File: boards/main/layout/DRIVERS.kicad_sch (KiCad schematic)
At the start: 28 parts, among them IC5 L6205D013TR, IC6 STSPIN958TR, M1 B02B-PASK(LF)(SN), M2 B02B-PASK(LF)(SN), M3 B02B-PASK(LF)(SN)

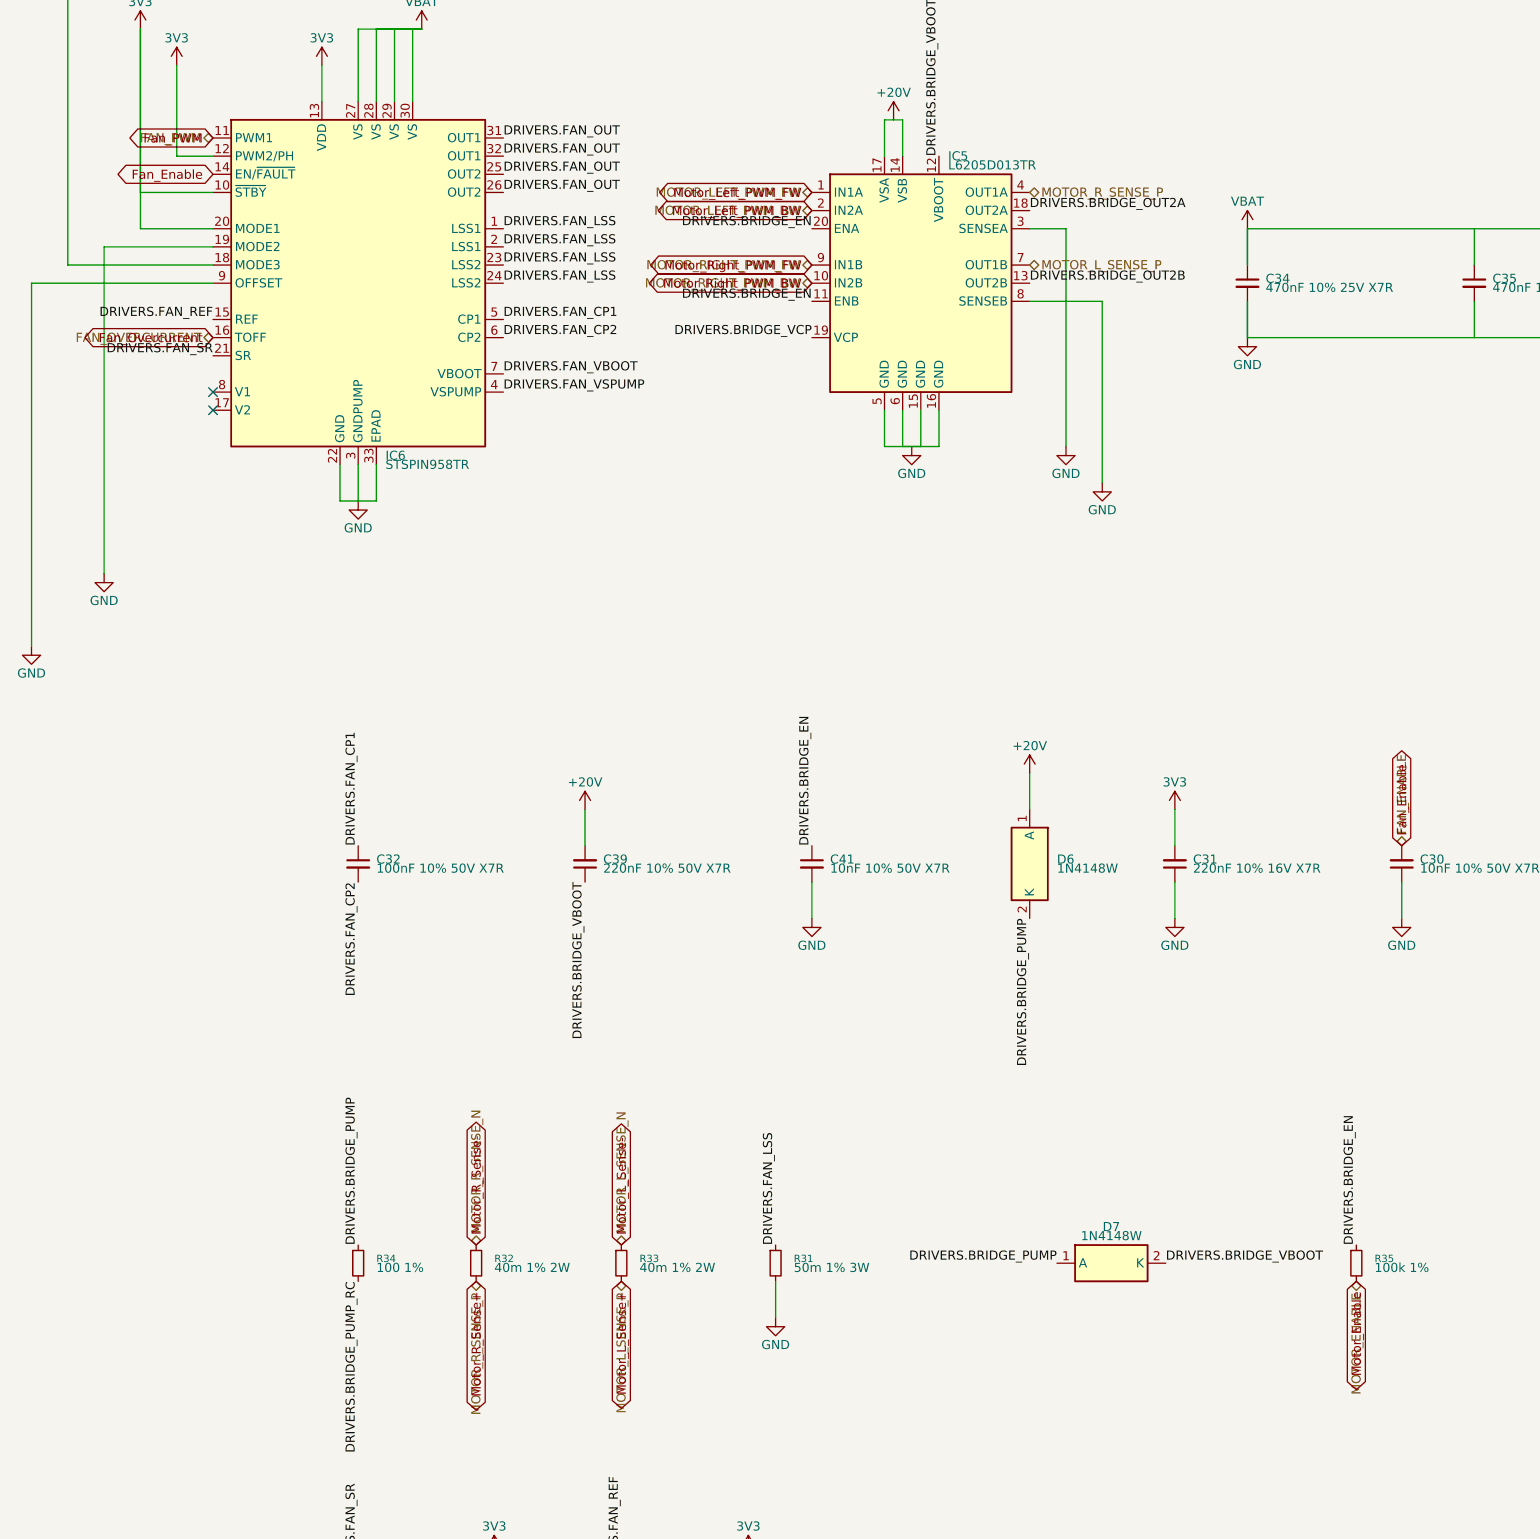
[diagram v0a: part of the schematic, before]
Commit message: 🏷️ Name the main board's module ports after their nets
A module's signal port now takes the name of the board net it carries (Fan_Enable, Wall_Sensor_0, Button), so its sheet pin and hierarchical label match the root's label: KiCad's ERC flagged each pair as similar_labels, names that differ only in case. The SPI buses and the Motor_*_Sense+/- nets, whose names are not identifiers, keep their port names. GND_BAT becomes a ground port of REGULATORS, so it reaches the root as a power symbol at the sheet pin instead of a dangling label. The netlist is unchanged: same nets, same names.
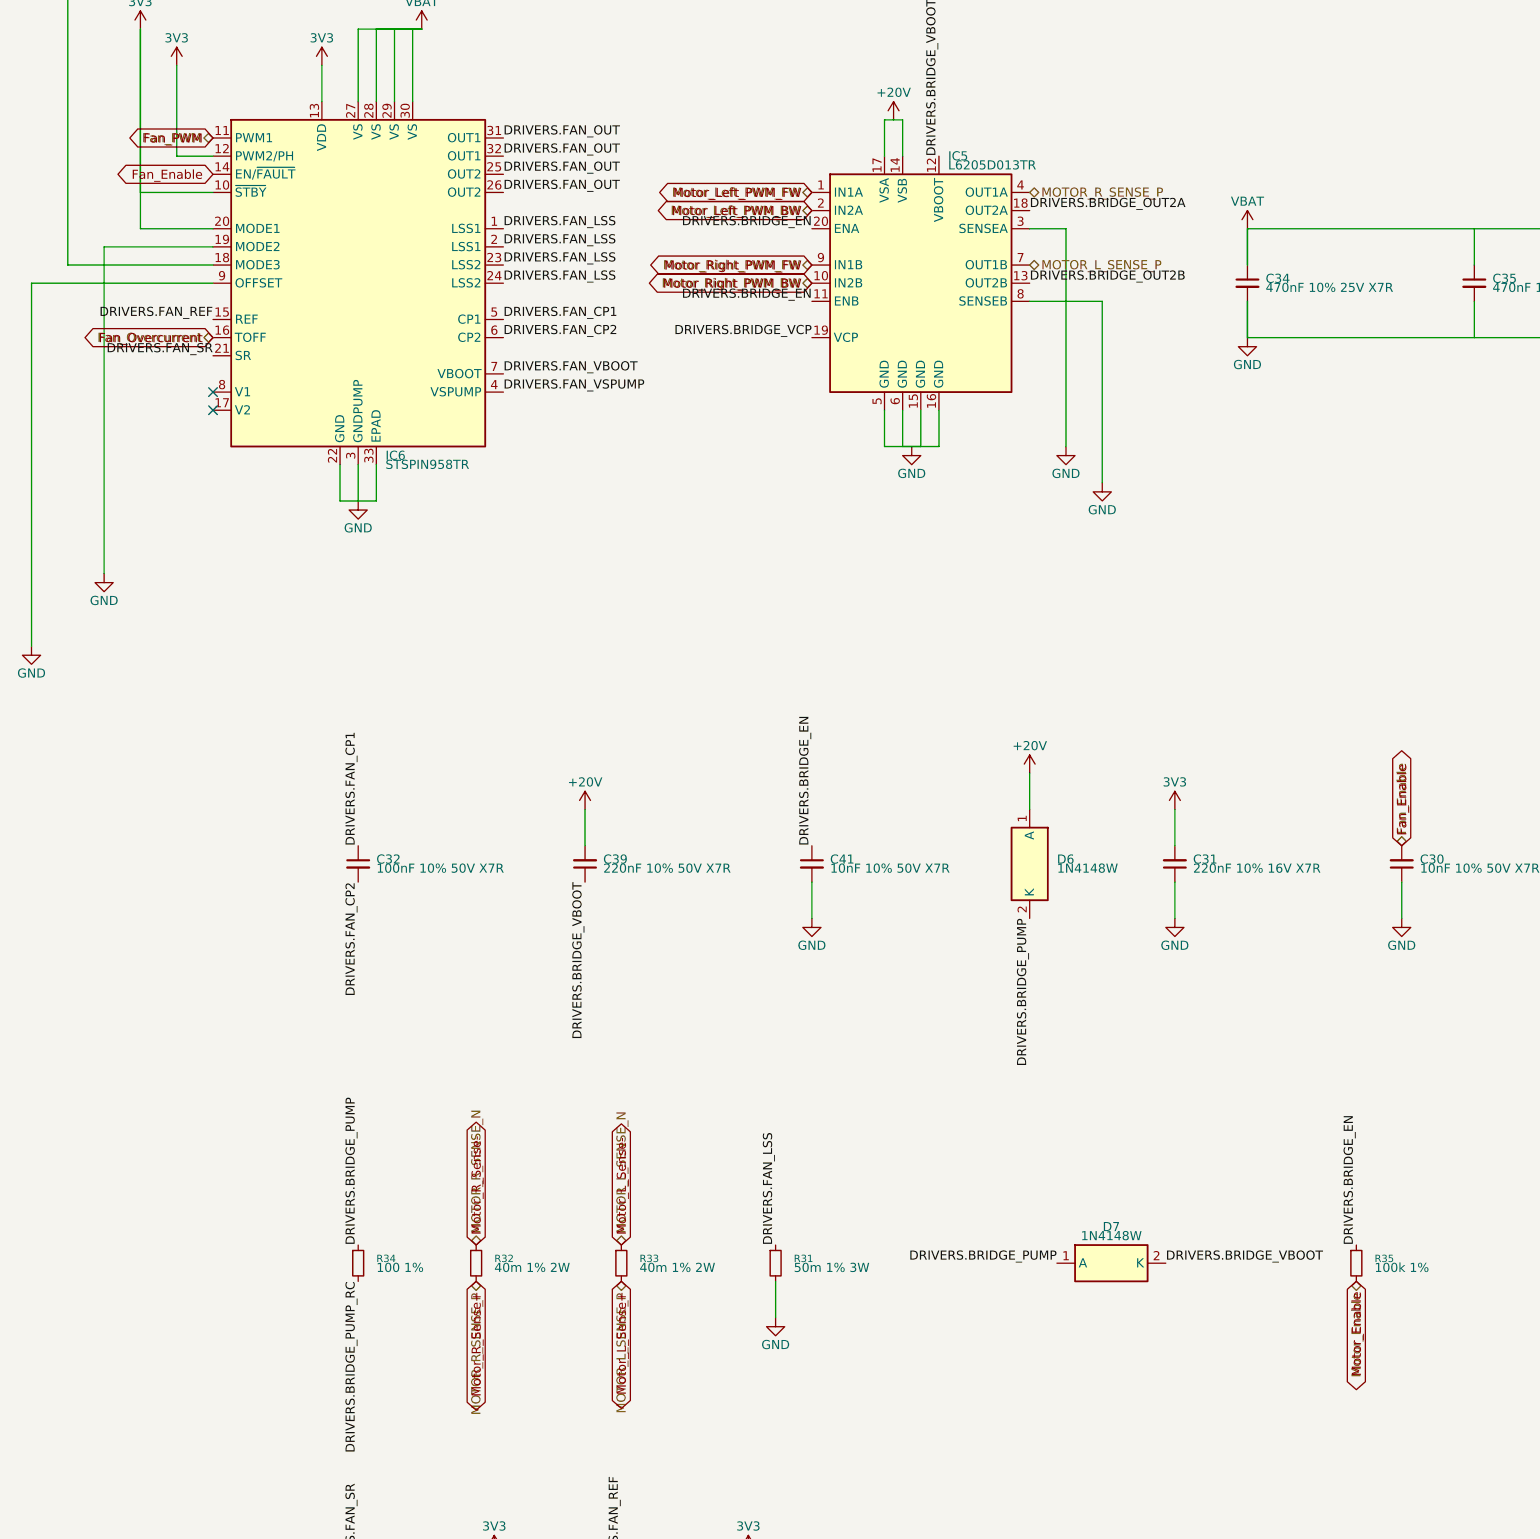
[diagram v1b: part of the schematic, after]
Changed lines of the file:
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@@
 		)
 	)
-	(hierarchical_label "MOTOR_RIGHT_PWM_FW"
+	(hierarchical_label "Motor_Left_PWM_FW"
 		(shape bidirectional)
-		(at 215.9 125.73 180)
+		(at 215.9 115.57 180)
 		(effects
 			(font
@@
 		)
 	)
-	(hierarchical_label "MOTOR_LEFT_PWM_BW"
+	(hierarchical_label "Fan_PWM"
 		(shape bidirectional)
-		(at 215.9 118.11 180)
+		(at 132.08 107.95 180)
 		(effects
 			(font
@@
 		)
 	)
+	(hierarchical_label "Fan_Enable"
+		(shape bidirectional)
+		(at 298.45 207.01 90)
+		(effects
+			(font
+				(size 1.27 1.27)
+			)
+			(justify left)
+		)
+	)
 	(hierarchical_label "MOTOR_R_SENSE_N"
 		(shape bidirectional)
@@
 		)
 	)
-	(hierarchical_label "MOTOR_ENABLE"
+	(hierarchical_label "Motor_Enable"
 		(shape bidirectional)
 		(at 292.1 267.97 270)
@@
 			)
 			(justify right)
-		)
-	)
-	(hierarchical_label "FAN_PWM"
-		(shape bidirectional)
-		(at 132.08 107.95 180)
-		(effects
-			(font
-				(size 1.27 1.27)
-			)
-			(justify right)
-		)
-	)
-	(hierarchical_label "FAN_OVERCURRENT"
-		(shape bidirectional)
-		(at 132.08 135.89 180)
-		(effects
-			(font
-				(size 1.27 1.27)
-			)
-			(justify right)
-		)
-	)
-	(hierarchical_label "FAN_ENABLE"
-		(shape bidirectional)
-		(at 298.45 207.01 90)
-		(effects
-			(font
-				(size 1.27 1.27)
-			)
-			(justify left)
 		)
 	)
@@
 		)
 	)
-	(hierarchical_label "MOTOR_LEFT_PWM_FW"
+	(hierarchical_label "Motor_Right_PWM_FW"
 		(shape bidirectional)
-		(at 215.9 115.57 180)
+		(at 215.9 125.73 180)
+		(effects
+			(font
+				(size 1.27 1.27)
+			)
+			(justify right)
+		)
+	)
+	(hierarchical_label "Motor_Left_PWM_BW"
+		(shape bidirectional)
+		(at 215.9 118.11 180)
+		(effects
+			(font
+				(size 1.27 1.27)
+			)
+			(justify right)
+		)
+	)
+	(hierarchical_label "Motor_Right_PWM_BW"
+		(shape bidirectional)
+		(at 215.9 128.27 180)
 		(effects
 			(font
@@
 		)
 	)
-	(hierarchical_label "MOTOR_RIGHT_PWM_BW"
+	(hierarchical_label "Fan_Overcurrent"
 		(shape bidirectional)
-		(at 215.9 128.27 180)
+		(at 132.08 135.89 180)
 		(effects
 			(font

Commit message: ✨ Place the schematics from per-sheet placement files
micras-pcb sch redraws each sheet pcb apply writes from
boards/<board>/schematic/<sheet>.toml: parts, wires, labels, power
symbols, titled frames, paper and title block, the root's sheet
symbols, and a ports column for the module sheets' extra labels. It
fails unless KiCad's netlist of the placed schematic equals pcb's.
make gen runs it after pcb apply; make check's sch gate fails on a part
without a placement, and tests/test_placement.py on any overlap.

The encoder and Bluetooth sheets are placed; the main board's DRIVERS
sheet is drafted.
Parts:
- added C65, C66: 10uF 10% 50V X5R, stdlib_kicad-footprints_Capacitor_SMD:C_0805_2012Metric, symbol C_Small
- added R49: 100k 1%, stdlib_kicad-footprints_Resistor_SMD:R_0402_1005Metric, symbol R_Small
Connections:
- net +20V: now also C65.2, C66.2
- net 3V3: no longer IC6.12 (PWM2/PH)
- net GND: now also IC6.12 (PWM2/PH), C65.1, C66.1, R49.1
- net Motor_L_Sense+: now also IC5.4 (OUT1A), R32.2; no longer IC5.7 (OUT1B), R33.2
- net Motor_L_Sense-: now also M1.2 (Pin_2), R32.1; no longer M2.2 (Pin_2), R33.1
- net Motor_R_Sense+: now also IC5.7 (OUT1B), R33.2; no longer IC5.4 (OUT1A), R32.2
- net Motor_R_Sense-: now also M2.2 (Pin_2), R33.1; no longer M1.2 (Pin_2), R32.1
- net Fan_Overcurrent renamed Fan_TOFF
- net Motor_Enable renamed Motors_Enable
- net Motors_Enable: now also R49.2
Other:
- note added: "Fan driver: STSPIN958, current limit through R31"
- note added: "Motor bridge: L6205, current sense through R32 and R33"
- note added: "Sheet ports"
- title: (none) -> Motor and fan drivers
- moved on the sheet: C30, C31, C32, C33, C34, C35, C36, C37, C38, C39, C40, C41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
